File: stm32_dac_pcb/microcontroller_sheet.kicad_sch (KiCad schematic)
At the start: 19 parts, among them J201 Conn_01x03, J202 Conn_01x05, J203 Conn_01x01, P201 USB_C_Plug_USB2.0, SW201 SW_Push, SW202 SW_Push, SW203 SW_Push, U101 STM32F411CEUx

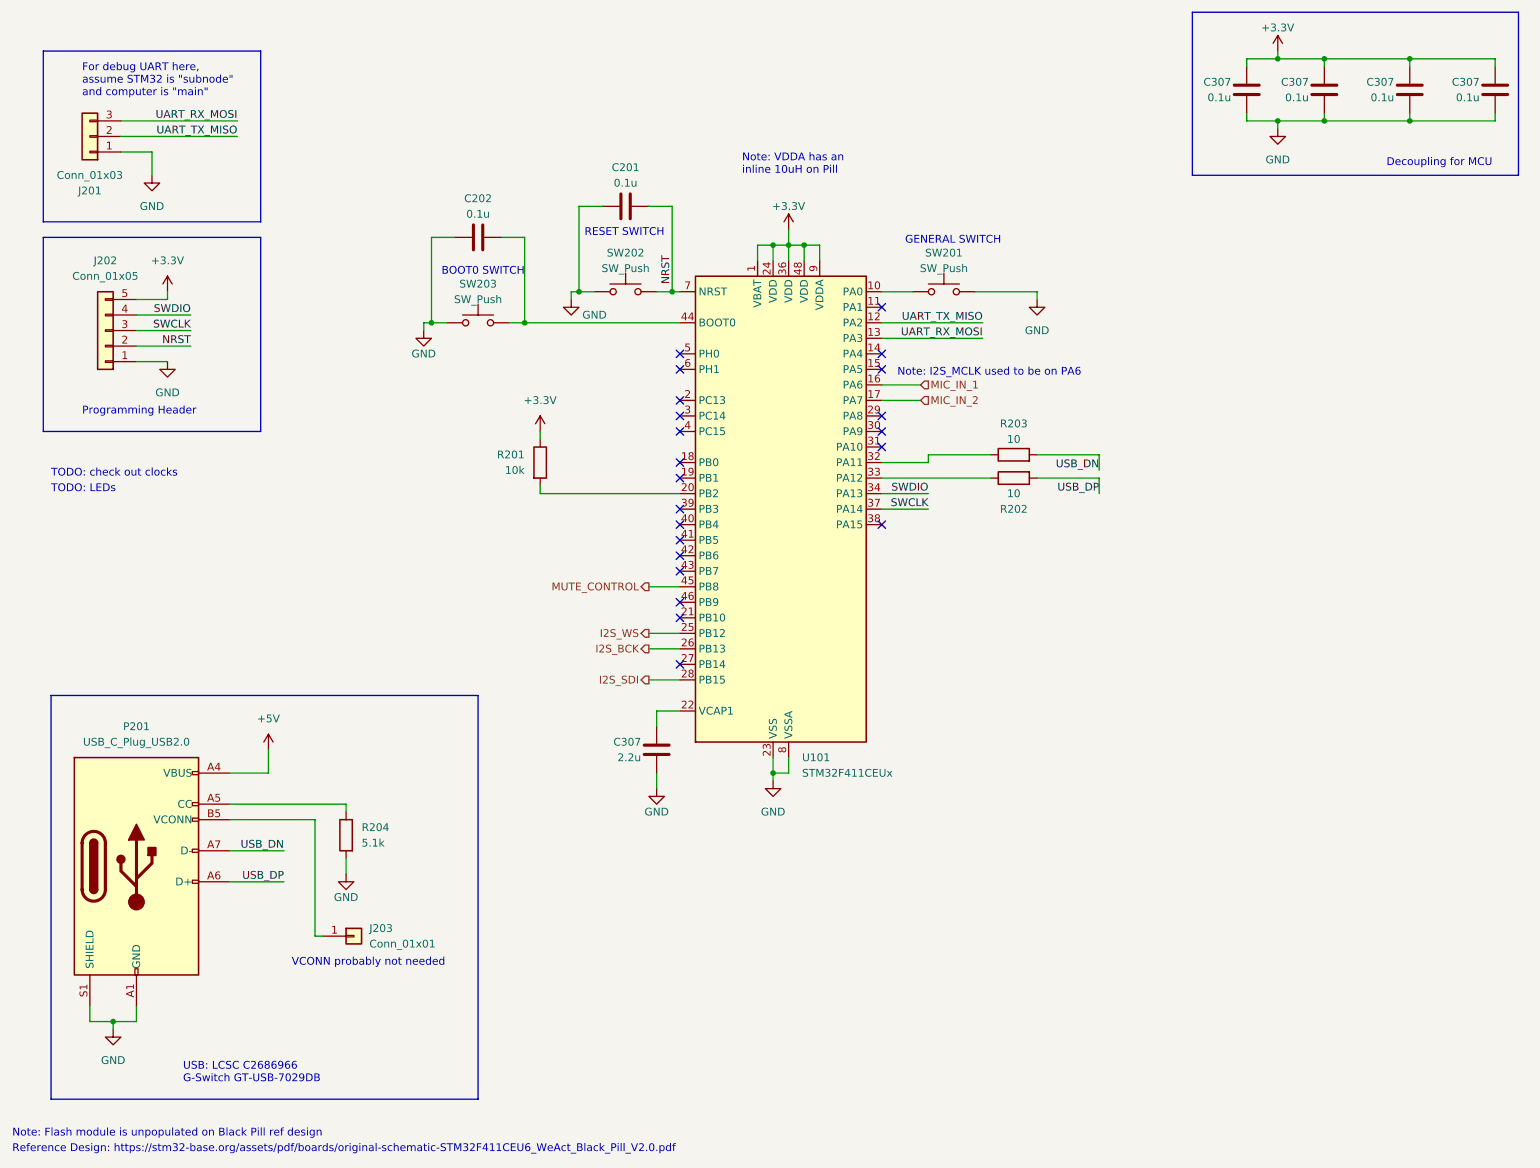
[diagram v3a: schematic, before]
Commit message: Fix USB connector, finish routing, export rev1 gerber
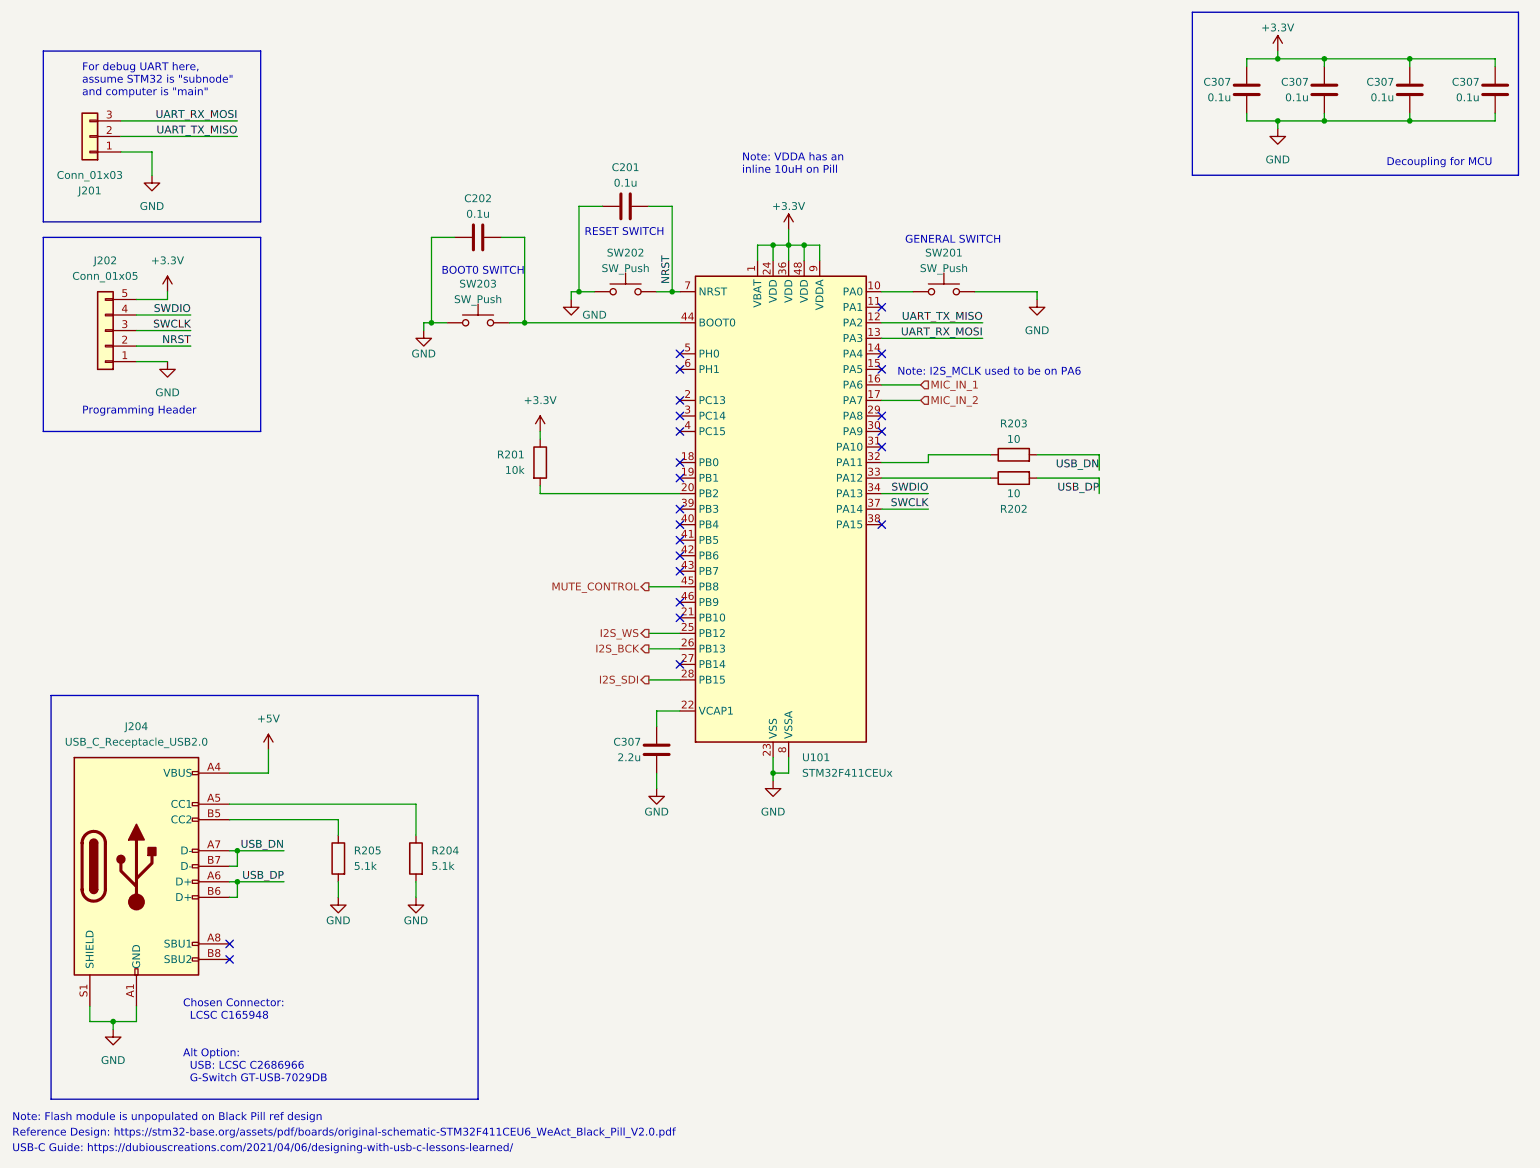
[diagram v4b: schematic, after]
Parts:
- removed J203: Conn_01x01, Connector_PinHeader_2.00mm:PinHeader_1x01_P2.00mm_Vertical, symbol Connector_Generic:Conn_01x01
- removed P201: USB_C_Plug_USB2.0, Connector_USB:USB_C_Receptacle_CNCTech_C-ARA1-AK51X, symbol Connector:USB_C_Plug_USB2.0
- added J204: USB_C_Receptacle_USB2.0, Connector_USB:USB_C_Receptacle_HRO_TYPE-C-31-M-12, symbol Connector:USB_C_Receptacle_USB2.0
- added R205: 5.1k, Resistor_SMD:R_0603_1608Metric_Pad0.98x0.95mm_HandSolder, symbol Device:R
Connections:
- net +5V: now also J204.A4 (VBUS), J204.A9 (VBUS), J204.B4 (VBUS), J204.B9 (VBUS)
- net GND: now also J204.A1 (GND), J204.A12 (GND), J204.B1 (GND), J204.B12 (GND), J204.S1 (SHIELD), R205.2
- net USB_DN: now also J204.A7 (D-), J204.B7 (D-)
- net USB_DP: now also J204.A6 (D+), J204.B6 (D+)
- net at R204.1: now also J204.A5 (CC1)
- new net: J204.B5 (CC2), R205.1
- no-connect marks 22 -> 24
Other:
- note added: "Chosen Connector: LCSC C165948 Alt Option: USB: LCSC C2686966 G-Switch GT-USB-7029DB"
- note added: "USB-C Guide: https://dubiouscreations.com/2021/04/06/designing-with-usb-c-lessons-learned/"
- note removed: "TODO: LEDs"
- note removed: "TODO: check out clocks"
- note removed: "USB: LCSC C2686966 G-Switch GT-USB-7029DB"
- note removed: "VCONN probably not needed"
- moved on the sheet: R204

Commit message: Fix rev1 generation with LCSC part num
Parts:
- J204: LCSC (none) -> C165948
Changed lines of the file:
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@@
+      (effects (font (size 1.27 1.27)) hide)
+    )
+    (property "LCSC" "C165948" (at 34.29 154.94 0)
       (effects (font (size 1.27 1.27)) hide)
     )
